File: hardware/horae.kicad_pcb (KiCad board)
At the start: 4 copper layers, 36.3 x 16.5 mm, 66 parts, among them J1 FH34SRJ-18S-0.5SH(50), Q1 AO3400A, SW1 UP/BOOT, SW2 DOWN, SW3 MENU, SW4 BACK, U1 ESP32-S3FN8, U2 TP4054, U3 RT9080-33, U4 USBLC6-2P6, U5 RV-3032-C7, U6 BMA400, Y1 40MHz 15pF

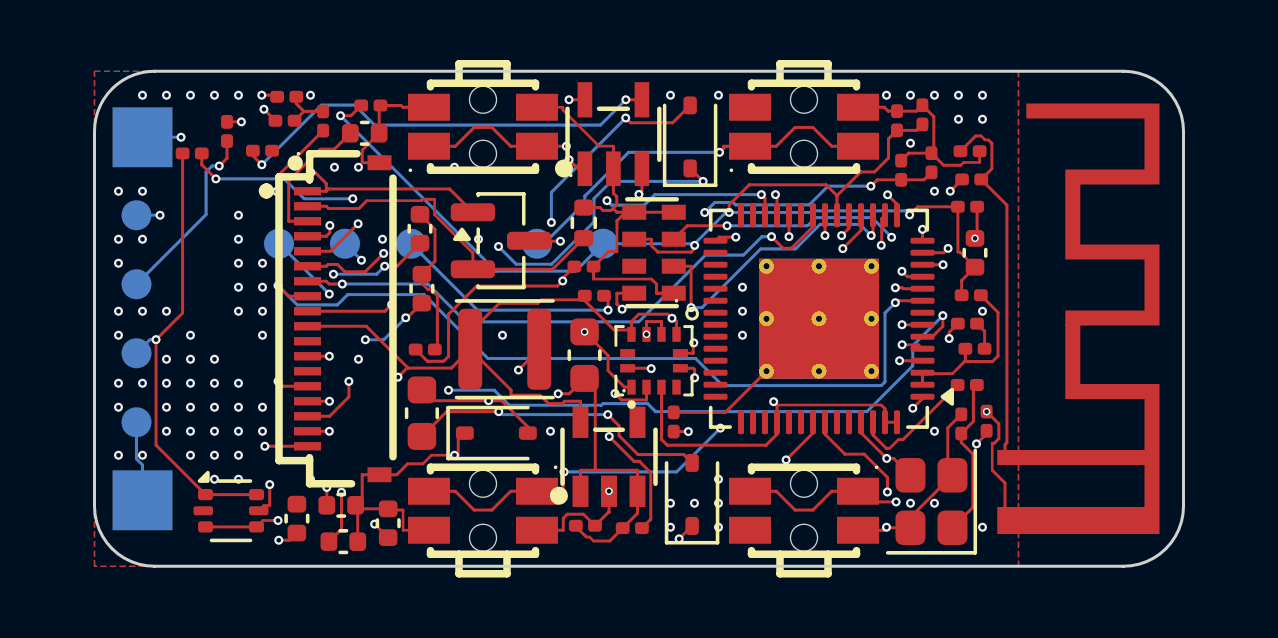
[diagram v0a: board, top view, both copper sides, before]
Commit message: Rev A: hand-routed 50-ohm RF feed, antenna clear of glass, standard vias, cost breakdown; splash-resistant PETG-CF case with TPU gaskets and PETG RF window
Co-Authored-By: Claude Opus 5.5 <noreply@anthropic.com>
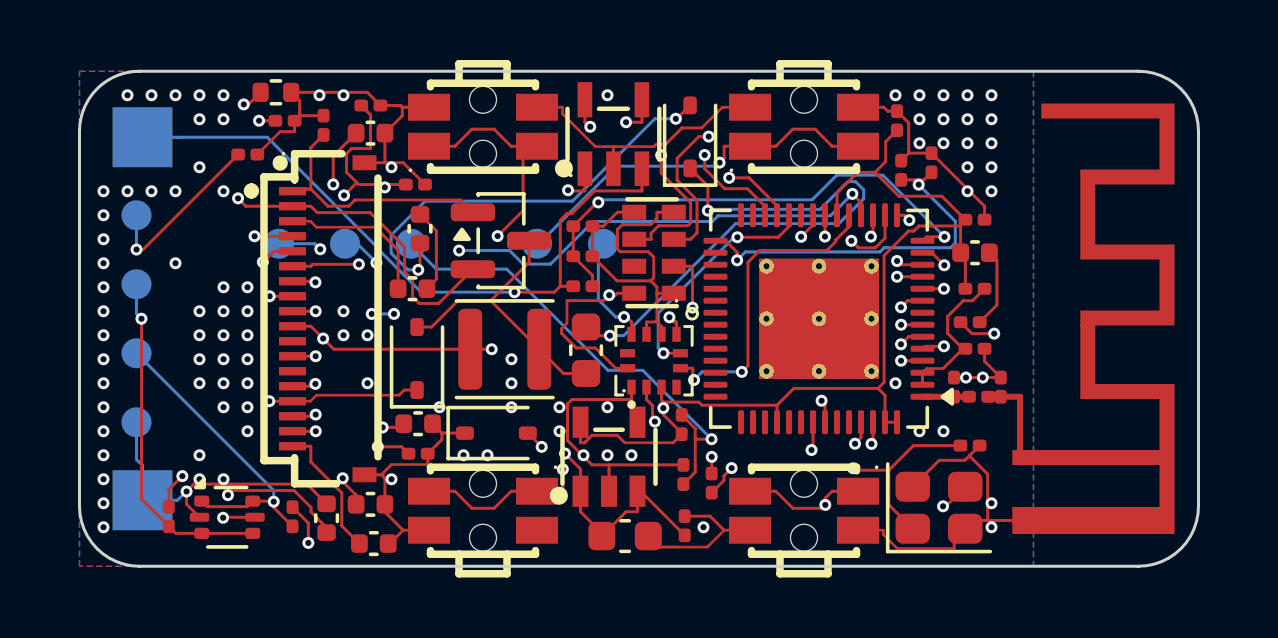
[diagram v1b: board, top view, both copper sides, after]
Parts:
- D1, D2, D3: value 1N5819WS -> B5819WS
- moved C19 17.1 mm to (92.5, 95.5), turned to 0 degrees
- moved R8 13.0 mm to (84.3, 106.6)
- moved R7 12.6 mm to (88.5, 106.6), turned to 90 degrees
- moved C28 11.5 mm to (92.6, 104.5), turned to 0 degrees
- moved R12 11.1 mm to (87.9, 92.5), turned to 0 degrees
- moved D3 10.2 mm to (92.6, 101.3)
- moved L1 9.12 mm to (102.4, 105.5), turned to 90 degrees
- moved R3 8.23 mm to (98.1, 98.9)
- moved C12 7.93 mm to (112.1, 102.3), turned to 90 degrees
- moved L3 7.25 mm to (111.3, 102.6)
- moved C15 6.18 mm to (99.5, 107.2), turned to 0 degrees
- moved R4 6.11 mm to (98.1, 97.9)
- moved C22 5.86 mm to (98.2, 101.0)
- moved C25 5.46 mm to (91.1, 93.8), turned to 0 degrees
- moved C26 5.42 mm to (92.5, 99.0)
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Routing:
- net GND: track 69.4 -> 94.9 mm, vias 93 -> 95
- net ESP_DP: track 20.7 -> 42.0 mm, vias 4 -> 2
- net BAT_ADC: track 33.8 -> 17.0 mm, vias 3 -> 2
- net I2C_SDA: track 30.2 -> 16.2 mm
- net ESP_DM: track 20.3 -> 31.0 mm
- net USB_DM: track 21.6 -> 11.4 mm, vias 2 -> 1
- net EPD_VSH1: track 15.0 -> 4.87 mm
- net EPD_SW: track 18.8 -> 9.53 mm, vias 4 -> 0
- net RF_ANT: track 12.4 -> 3.08 mm
- net RF_CHIP: track 9.71 -> 1.55 mm, vias 3 -> 0
- net XTAL_P: track 5.42 -> 12.9 mm, vias 0 -> 2
- net RTC_INT: track 10.5 -> 17.7 mm, vias 3 -> 2
- net XTAL_N: track 6.35 -> 13.3 mm, vias 2 -> 3
- net PREVGH: track 20.5 -> 15.2 mm, vias 4 -> 2
- net EPD_RES: track 25.4 -> 30.7 mm
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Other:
- board size 36.3 x 16.5 mm -> 37.3 x 16.5 mm

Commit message: Rev A: antenna trimmed 6.64 mm + re-matched from openEMS sim (C11 0.9p, L3 0.6n, C12 DNP); timeline entry with review renders
Co-Authored-By: Claude Opus 5.5 <noreply@anthropic.com>
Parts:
- C1, C2: value 22pF -> 24pF
- C11: value 3pF -> 0.9pF
- C12: value 3pF -> DNP
- L3: value 7.5nH -> 0.6nH

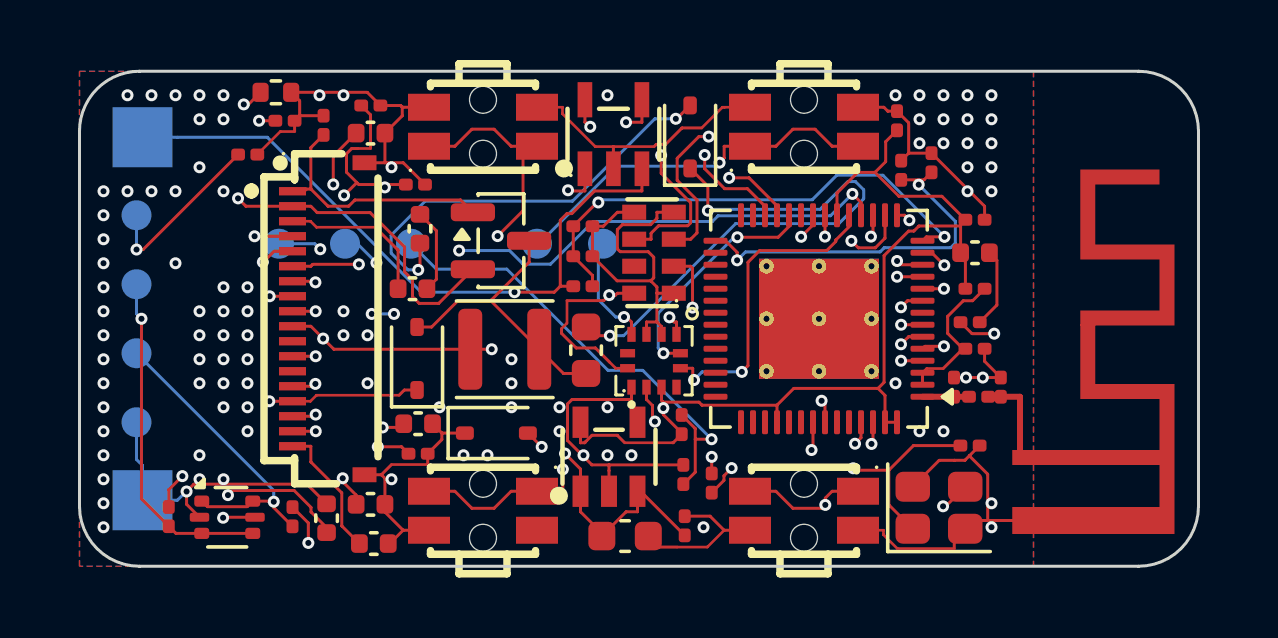
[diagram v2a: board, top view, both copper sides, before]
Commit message: Rev A: haptics back (spring-contact coin ERM + CJ3134K), LIS2DUX12 replaces BMA400 (-$10.9/board), GND escape vias, hole-to-hole spacing; DRC clean
Co-Authored-By: Claude Opus 5.5 <noreply@anthropic.com>
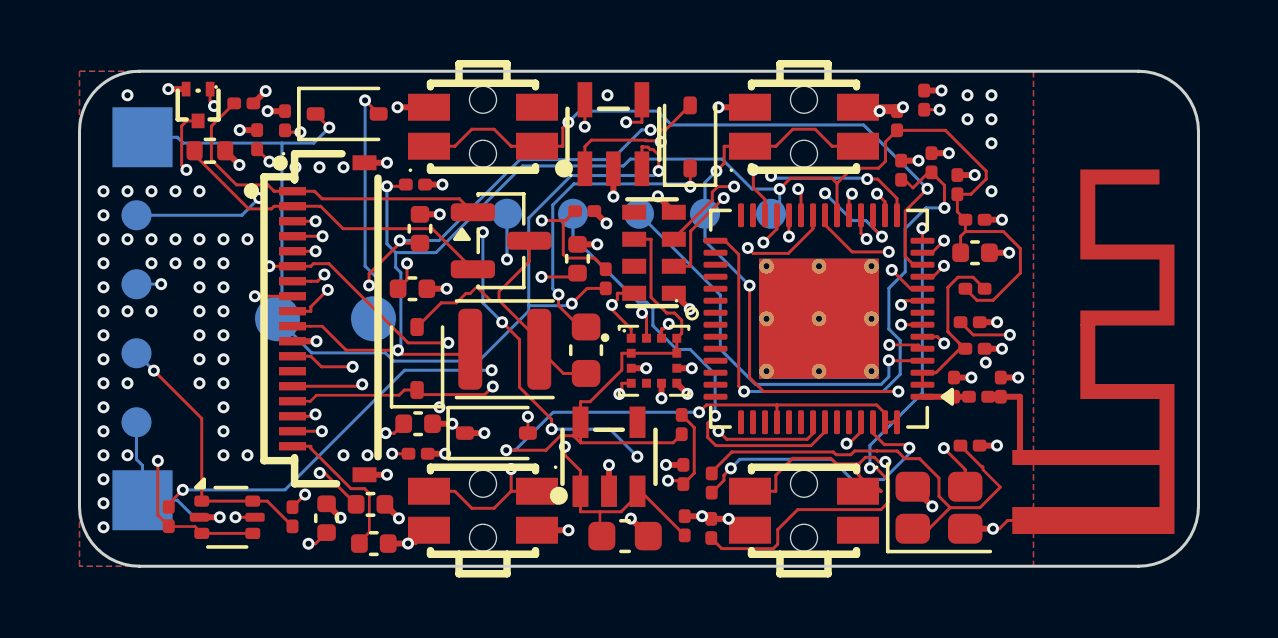
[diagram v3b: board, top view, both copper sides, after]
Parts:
- added D4: B5819WS, Diode_SMD:D_SOD-323, F.Cu at (90.3, 93.2)
- added Q2: CJ3134K, horae:SOT-723_L1.2-W0.8-P0.40-LS1.2-BR, F.Cu at (85.3, 92.9)
- added R13: 1M, Resistor_SMD:R_0201_0603Metric, F.Cu at (109.5, 92.7)
- added TP7: VBAT, TestPoint:TestPoint_Pad_D1.5mm, B.Cu at (88.0, 100.0)
- added TP8: MOT_N, TestPoint:TestPoint_Pad_D1.5mm, B.Cu at (91.2, 100.0)
- U6: value BMA400 -> LIS2DUX12; footprint horae:LGA-12_L2.0-W2.0-P0.50-BL -> horae:LGA-12_L2.0-W2.0-P0.50-TL_LIS2DUX12TR
- moved C20 19.7 mm to (110.6, 95.5), turned to 90 degrees
- moved R4 10.0 mm to (102.4, 107.0), turned to 90 degrees
- moved C25 8.07 mm to (98.0, 98.0), turned to 90 degrees
- moved TP10 7.67 mm to (97.8, 96.5)
- moved TP11 7.67 mm to (100.0, 96.5)
- moved TP9 7.67 mm to (95.6, 96.5)
- moved TP12 5.69 mm to (102.2, 96.5)
- moved TP13 5.69 mm to (104.4, 96.5)
- moved R12 2.94 mm to (85.7, 94.4)
- moved R11 2.76 mm to (86.8, 92.8), turned to 0 degrees
- moved R3 0.80 mm to (98.9, 98.7), turned to 90 degrees
- moved C13 0.59 mm to (87.3, 94.0), turned to 90 degrees
- moved C18 0.51 mm to (98.2, 96.4)
- turned R2 to 90 degrees
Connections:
- U1 pad 23: (no net) -> VIB
- U6 pad 1: GND -> I2C_SCL
- U6 pad 11: (no net) -> ACC_INT2
- U6 pad 12: I2C_SCL -> ACC_INT1
- U6 pad 2: I2C_SDA -> +3V3
- U6 pad 3: +3V3 -> GND
- U6 pad 4: (no net) -> I2C_SDA
- U6 pad 5: ACC_INT1 -> (no net)
- U6 pad 6: ACC_INT2 -> GND
- U6 pad 7: +3V3 -> GND
- U6 pad 9: GND -> +3V3
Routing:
- net GND: track 94.9 -> 42.7 mm, vias 95 -> 112
- net VIB: track 0.00 -> 35.3 mm, vias 0 -> 3
- net RTC_INT: track 17.7 -> 40.5 mm, vias 2 -> 6
- net BAT_ADC: track 17.0 -> 37.2 mm, vias 2 -> 3
- net MOT_N: track 0.00 -> 17.3 mm, vias 0 -> 2
- net EPD_DC: track 19.2 -> 35.3 mm, vias 2 -> 3
- net ESP_DP: track 42.0 -> 29.5 mm
- net BTN_BACK: track 20.5 -> 30.9 mm
- net VBAT: track 38.0 -> 48.0 mm, vias 2 -> 4
- net I2C_SDA: track 16.2 -> 25.5 mm, vias 3 -> 4
- net RXD0: track 23.1 -> 14.5 mm, vias 2 -> 1
- net VDD_SPI: track 12.4 -> 20.6 mm
- net TXD0: track 23.3 -> 15.9 mm, vias 4 -> 2
- net PREVGL: track 26.4 -> 20.6 mm, vias 3 -> 4
- net EPD_MOSI: track 23.8 -> 29.3 mm, vias 3 -> 2
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
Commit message: Rev A: capacitive touch (no switches), 6 mm spring-contact motor, full-size battery (25.3x16x2.5), pogo/battery pads in motor-zone corners, PPG hookup pads, RF router class; DRC clean
Co-Authored-By: Claude Opus 5.5 <noreply@anthropic.com>
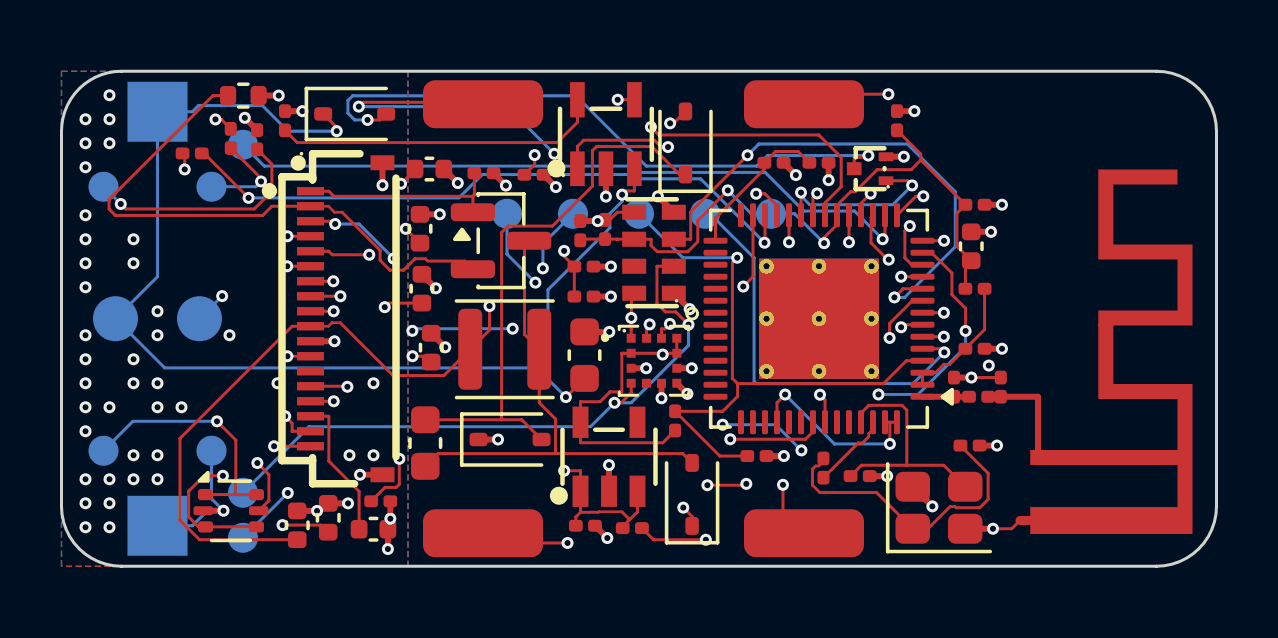
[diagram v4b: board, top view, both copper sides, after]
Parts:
- removed SW1: UP/BOOT, horae:SW-SMD_L3.5-W2.9_EVQ-P7M01P
- removed SW2: DOWN, horae:SW-SMD_L3.5-W2.9_EVQ-P7M01P
- removed SW3: MENU, horae:SW-SMD_L3.5-W2.9_EVQ-P7M01P
- removed SW4: BACK, horae:SW-SMD_L3.5-W2.9_EVQ-P7M01P
- added TCH1: TOUCH_UP, horae:TouchPad_4.0x1.6mm, F.Cu at (105.5, 92.8)
- added TCH2: TOUCH_DOWN, horae:TouchPad_4.0x1.6mm, F.Cu at (105.5, 107.2)
- added TCH3: TOUCH_MENU, horae:TouchPad_4.0x1.6mm, F.Cu at (94.8, 92.8)
- added TCH4: TOUCH_BACK, horae:TouchPad_4.0x1.6mm, F.Cu at (94.8, 107.2)
- added TP14: I2C_SDA, TestPoint:TestPoint_Pad_D1.0mm, B.Cu at (86.8, 105.8)
- added TP15: I2C_SCL, TestPoint:TestPoint_Pad_D1.0mm, B.Cu at (86.8, 94.2)
- added TP16: PPG_INT, TestPoint:TestPoint_Pad_D1.0mm, B.Cu at (86.8, 107.3)
- TP12: value BTN_UP -> BOOT
- moved Q2 22.5 mm to (107.7, 95.0), turned to 0 degrees
- moved R13 13.2 mm to (96.5, 95.2), turned to 0 degrees
- moved R8 12.8 mm to (86.4, 94.0)
- moved C20 12.7 mm to (98.0, 97.1)
- moved R7 12.6 mm to (85.1, 94.5), turned to 0 degrees
- moved D3 10.2 mm to (101.8, 105.9)
- moved R4 8.82 mm to (98.2, 99.3), turned to 0 degrees
- moved C27 8.50 mm to (93.0, 95.0)
- moved R3 8.36 mm to (99.8, 107.0), turned to 0 degrees
- moved R11 8.34 mm to (94.8, 95.2)
- moved C19 6.49 mm to (98.9, 97.0), turned to 90 degrees
- moved C2 6.31 mm to (107.4, 105.2)
- moved C22 6.19 mm to (92.9, 104.1)
- moved C15 6.18 mm to (98.2, 101.2), turned to 90 degrees
- moved TP8 5.80 mm to (85.3, 100.0)
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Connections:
- net BTN_UP renamed BOOT
- U1 pad 11: BTN_BACK -> TOUCH_BACK
- U1 pad 12: BTN_MENU -> TOUCH_MENU
- U1 pad 13: BTN_DOWN -> TOUCH_DOWN
- U1 pad 19: ACC_INT1 -> PPG_INT
- U1 pad 24: ACC_INT2 -> ACC_INT1
- U1 pad 27: (no net) -> ACC_INT2
- U1 pad 8: (no net) -> TOUCH_UP
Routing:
- net BTN_BACK: track 30.9 -> 0.00 mm, vias 2 -> 0
- net PPG_INT: track 0.00 -> 28.8 mm, vias 0 -> 2
- net TOUCH_MENU: track 0.00 -> 26.7 mm, vias 0 -> 3
- net RTC_INT: track 40.5 -> 17.5 mm, vias 6 -> 2
- net BTN_MENU: track 22.3 -> 0.00 mm, vias 2 -> 0
- net TOUCH_BACK: track 0.00 -> 19.9 mm, vias 0 -> 2
- net I2C_SCL: track 15.1 -> 34.9 mm
- net VIB: track 35.3 -> 16.9 mm
- net BTN_DOWN: track 16.7 -> 0.00 mm, vias 2 -> 0
- net VDD_SPI: track 20.6 -> 5.09 mm, vias 2 -> 0
- net MOT_N: track 17.3 -> 31.8 mm, vias 2 -> 3
- net +3V3: track 91.0 -> 77.0 mm
- net TOUCH_DOWN: track 0.00 -> 13.9 mm, vias 0 -> 3
- net TOUCH_UP: track 0.00 -> 12.2 mm, vias 0 -> 2
- net BOOT: track 25.7 -> 13.9 mm, vias 4 -> 1
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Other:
- board size 37.3 x 16.5 mm -> 38.5 x 16.5 mm

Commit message: Rev A: top-port PDM mic (LMD2718T261, GPIO-powered, 0 uA off) in the -X corner; DRC clean
Co-Authored-By: Claude Opus 5.5 <noreply@anthropic.com>
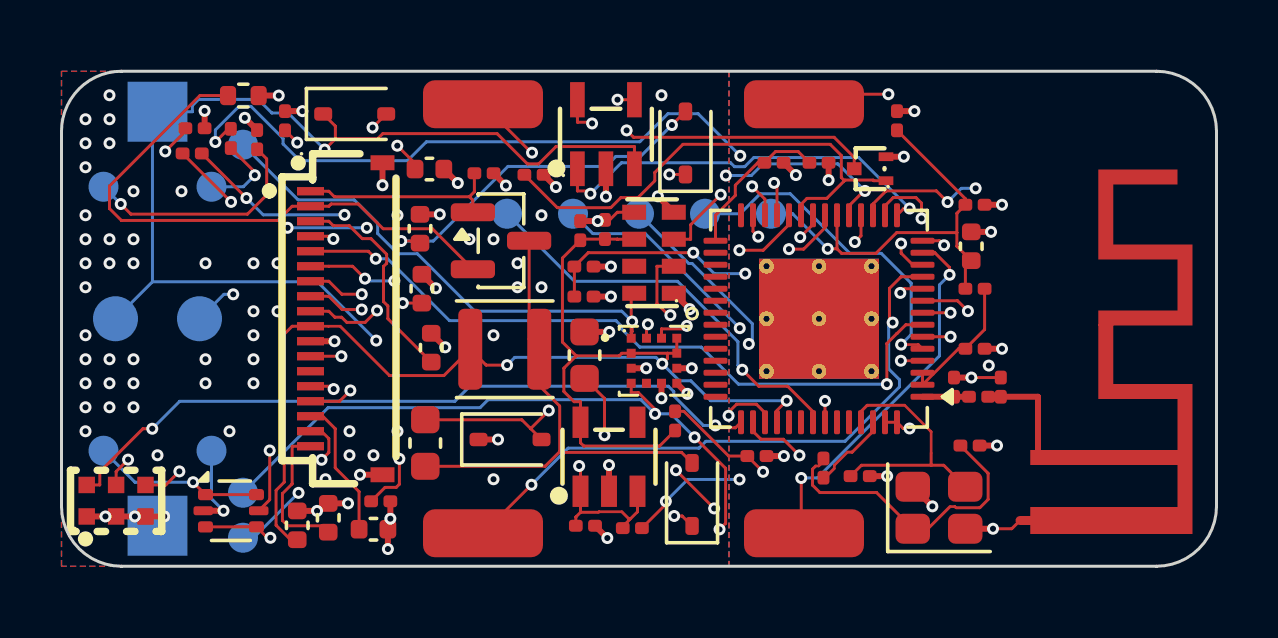
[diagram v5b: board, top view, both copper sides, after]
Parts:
- added C31: 100nF, Capacitor_SMD:C_0201_0603Metric, F.Cu at (85.2, 93.7)
- added MIC1: LMD2718T261, horae:MIC-SMD_6P-L2.8-W1.9-P0.98-TL, F.Cu at (82.6, 106.1)
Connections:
- U1 pad 43: (no net) -> MIC_VDD
- U1 pad 44: (no net) -> MIC_CLK
- U1 pad 45: (no net) -> MIC_DATA
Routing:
- net MIC_VDD: track 0.00 -> 34.6 mm, vias 0 -> 3
- net MIC_CLK: track 0.00 -> 29.8 mm, vias 0 -> 2
- net MIC_DATA: track 0.00 -> 27.0 mm, vias 0 -> 2
- net I2C_SDA: track 32.1 -> 50.1 mm, vias 3 -> 6
- net ESP_DM: track 39.8 -> 23.6 mm, vias 2 -> 3
- net TOUCH_MENU: track 26.7 -> 17.4 mm, vias 3 -> 2
- net +3V3: track 77.0 -> 69.5 mm, vias 6 -> 5
- net USB_DM: track 18.2 -> 23.7 mm
- net MOT_N: track 31.8 -> 26.6 mm
- net EPD_CS: track 19.1 -> 24.2 mm
- net VBAT: track 48.0 -> 52.8 mm
- net PPG_INT: track 28.8 -> 33.4 mm, vias 2 -> 5
- net EPD_BUSY: track 34.2 -> 29.8 mm
- net EN: track 20.4 -> 24.3 mm, vias 1 -> 3
- net EPD_RES: track 27.5 -> 23.9 mm, vias 6 -> 2
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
